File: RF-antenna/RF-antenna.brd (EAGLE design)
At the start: 108.2 x 108.2 mm, 7 parts, among them X1 SMA-V, X2 SMA-V, X3 SMA-V, X4 SMA-V, X5 SMA-V, X6 SMA-V

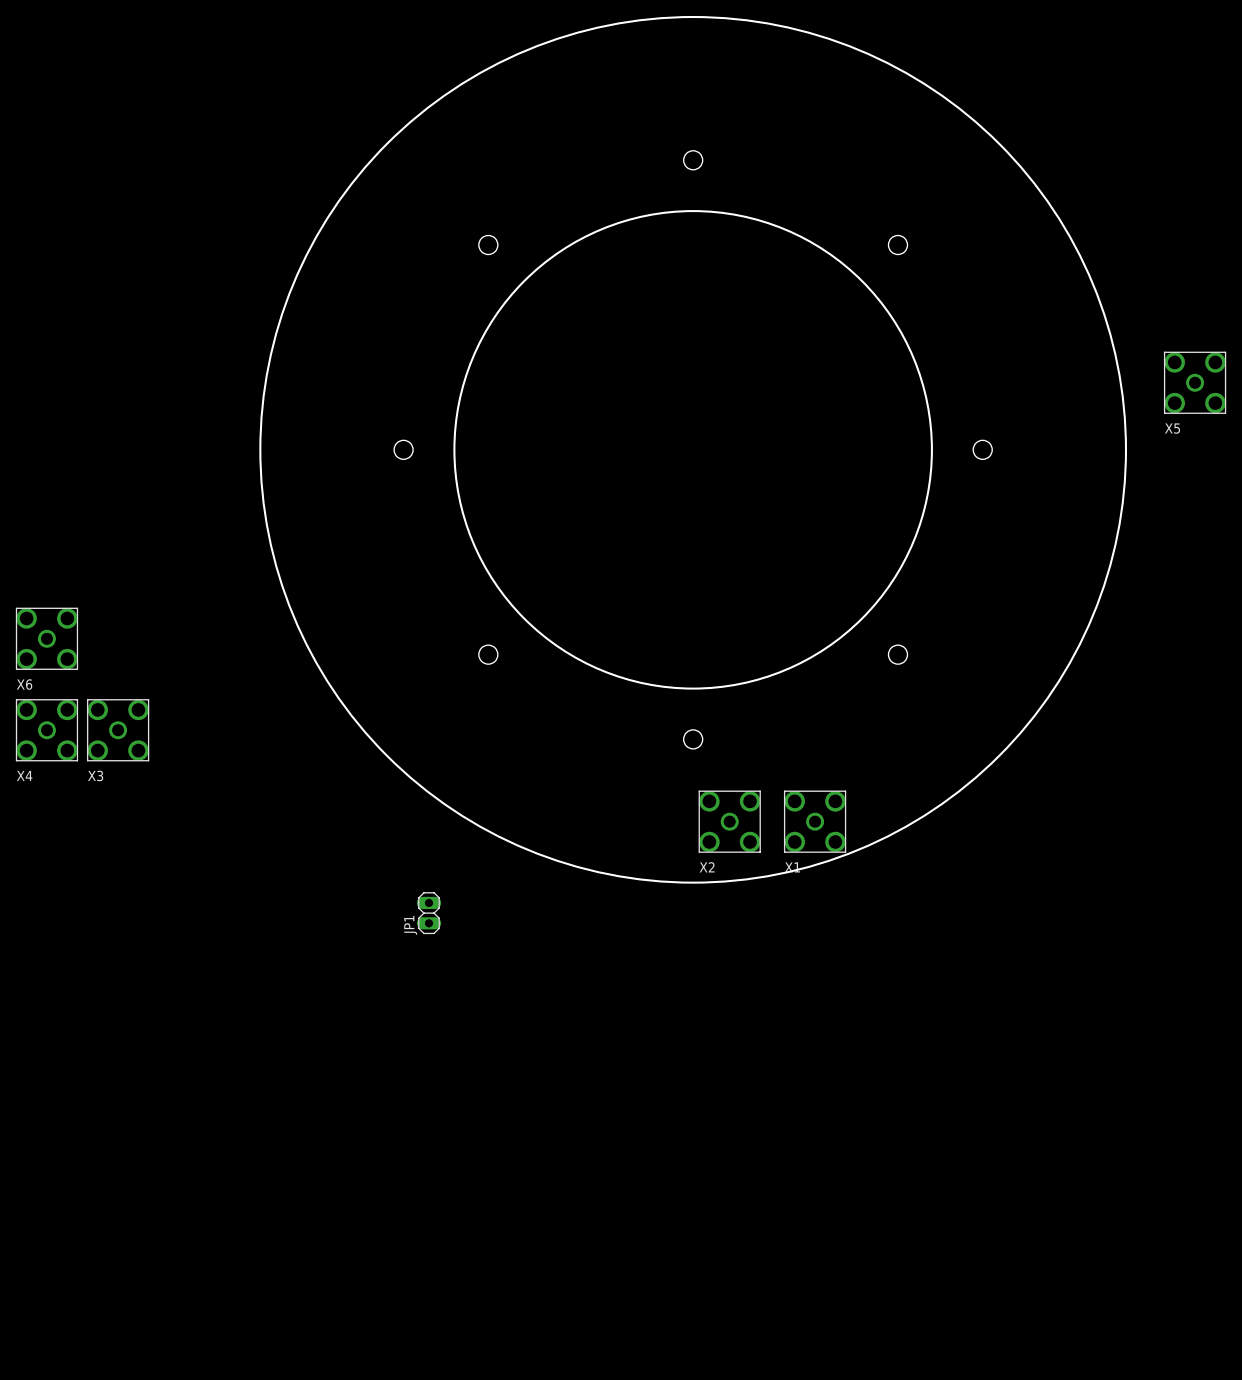
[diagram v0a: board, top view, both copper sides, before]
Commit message: Adding parts for footprinting
Added a bunch of test components to get an idea of how tight the design
will be. Also corrected the keepout areas.

DSB
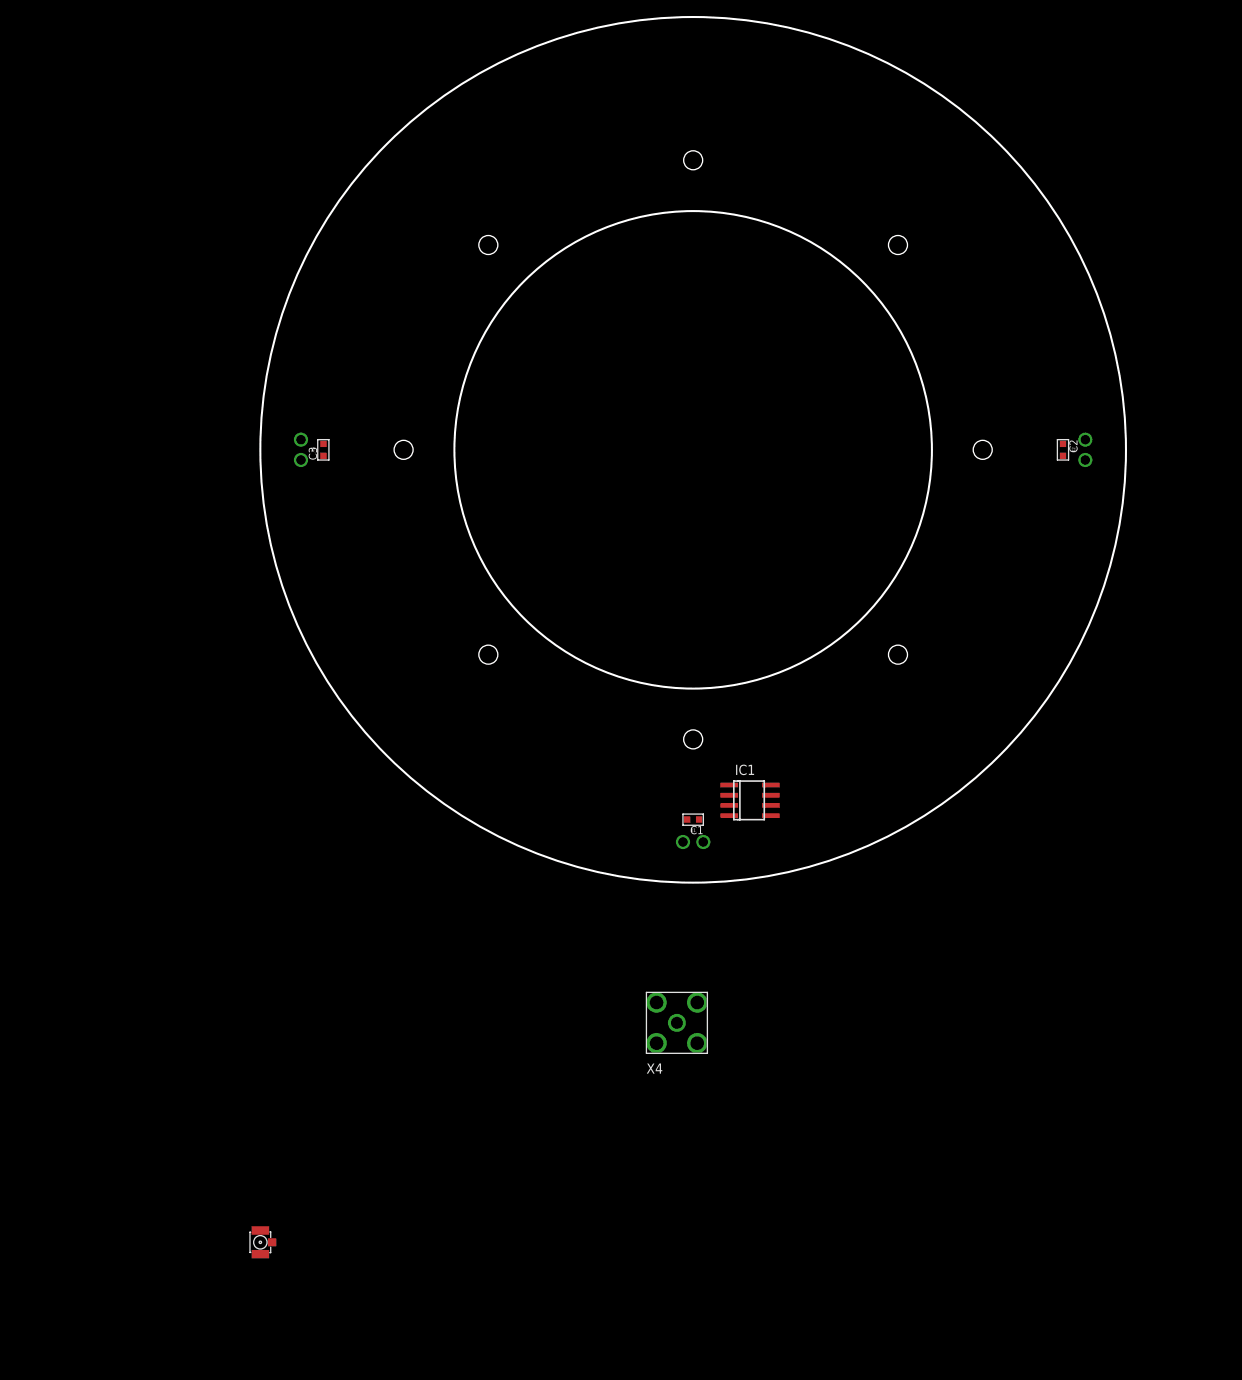
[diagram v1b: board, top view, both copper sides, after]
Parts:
- removed JP1: (no value), pinhead:1X02
- removed X5, X6: SMA-V, connector-jqi:SMA-V
- added C1, C2, C3: 5 pF, jqi_passives:C_MLCC_0603
- added CON1: UMC_CONNECTORREGULAR, qkdlab_alessandro:UMC_CONNECTOR
- added IC1: (no value), opamp-jqi:SO08
- X1, X2, X3: value SMA-V -> LG_HEADER; device connector-jqi:SMA-V -> connector-jqi:LG_HEADER
- moved X4 86.8 mm to (52.1, -17.5)
- moved X2 64.3 mm to (103.1, 54.1), turned to 90 degrees
- moved X3 41.8 mm to (5.08, 54.1), turned to 270 degrees
- moved X1 15.5 mm to (54.1, 5.08)
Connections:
- removed net GND: X1.GND1, X1.GND2, X1.GND3, X1.GND4, X2.GND1, X2.GND2, X2.GND3, X2.GND4
- new net N$2: C2.P$1, C2.P$2, X2.I, X2.R
- new net N$3: C3.P$1, C3.P$2, X3.I, X3.R
- new net V+: IC1.7
- new net V-: IC1.4
- net N$1: now also C1.P$1, C1.P$2, X1.I, X1.R; no longer X1.RF, X2.RF
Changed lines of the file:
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@@
 <?xml version="1.0" encoding="utf-8"?>
 <!DOCTYPE eagle SYSTEM "eagle.dtd">
-<eagle version="7.7.0">
+<eagle version="8.5.0">
 <drawing>
 <settings>
 <setting alwaysvectorfont="no"/>
+<setting keepoldvectorfont="yes"/>
 <setting verticaltext="up"/>
 </settings>
-<grid distance="0.01" unitdist="inch" unit="inch" style="lines" multiple="1" display="yes" altdistance="0.001" altunitdist="inch" altunit="inch"/>
+<grid distance="0.01" unitdist="inch" unit="inch" style="dots" multiple="1" display="yes" altdistance="0.001" altunitdist="inch" altunit="inch"/>
 <layers>
 <layer number="1" name="Top" color="4" fill="1" visible="yes" active="yes"/>
@@
 <circle x="54.102" y="54.102" radius="29.845" width="0.254" layer="20"/>
 <circle x="54.102" y="54.102" radius="54.102" width="0.254" layer="20"/>
-<wire x1="92.964" y1="54.102" x2="108.204" y2="61.722" width="0.254" layer="40"/>
-<wire x1="108.204" y1="61.722" x2="108.204" y2="46.482" width="0.254" layer="40"/>
-<wire x1="108.204" y1="46.482" x2="92.964" y2="54.102" width="0.254" layer="40"/>
-<wire x1="54.102" y1="92.964" x2="61.722" y2="108.204" width="0.254" layer="40"/>
-<wire x1="61.722" y1="108.204" x2="46.482" y2="108.204" width="0.254" layer="40"/>
-<wire x1="46.482" y1="108.204" x2="54.102" y2="92.964" width="0.254" layer="40"/>
-<wire x1="15.494" y1="54.102" x2="0" y2="46.482" width="0.254" layer="40"/>
-<wire x1="0" y1="46.482" x2="0" y2="61.722" width="0.254" layer="40"/>
-<wire x1="0" y1="61.722" x2="15.494" y2="54.102" width="0.254" layer="40"/>
-<wire x1="54.102" y1="15.494" x2="61.722" y2="0" width="0.254" layer="40"/>
-<wire x1="61.722" y1="0" x2="46.482" y2="0" width="0.254" layer="40"/>
-<wire x1="46.482" y1="0" x2="54.102" y2="15.494" width="0.254" layer="40"/>
 <hole x="90.297" y="54.102" drill="2.3749"/>
 <hole x="54.102" y="90.297" drill="2.3749"/>
@@
 <wire x1="70.104" y1="0" x2="70.104" y2="108.204" width="0.254" layer="39"/>
 <wire x1="70.104" y1="108.204" x2="38.1" y2="108.204" width="0.254" layer="39"/>
+<polygon width="0.254" layer="40" pour="hatch">
+<vertex x="96.774" y="60.96"/>
+<vertex x="106.934" y="66.04"/>
+<vertex x="107.188" y="65.024"/>
+<vertex x="107.442" y="63.754"/>
+<vertex x="107.696" y="62.23"/>
+<vertex x="107.95" y="60.706"/>
+<vertex x="108.204" y="57.912"/>
+<vertex x="108.204" y="54.102"/>
+<vertex x="108.204" y="50.292"/>
+<vertex x="107.95" y="47.752"/>
+<vertex x="107.696" y="45.974"/>
+<vertex x="107.442" y="44.45"/>
+<vertex x="107.188" y="43.18"/>
+<vertex x="106.934" y="42.164"/>
+<vertex x="96.774" y="47.244"/>
+<vertex x="97.028" y="49.276"/>
+<vertex x="97.282" y="52.832"/>
+<vertex x="97.282" y="54.102"/>
+<vertex x="97.282" y="55.372"/>
+<vertex x="97.028" y="58.928"/>
+</polygon>
+<polygon width="0.254" layer="40" pour="hatch">
+<vertex x="47.244" y="96.774"/>
+<vertex x="42.164" y="106.934"/>
+<vertex x="43.18" y="107.188"/>
+<vertex x="44.45" y="107.442"/>
+<vertex x="45.974" y="107.696"/>
+<vertex x="47.498" y="107.95"/>
+<vertex x="50.292" y="108.204"/>
+<vertex x="54.102" y="108.204"/>
+<vertex x="57.912" y="108.204"/>
+<vertex x="60.452" y="107.95"/>
+<vertex x="62.23" y="107.696"/>
+<vertex x="63.754" y="107.442"/>
+<vertex x="65.024" y="107.188"/>
+<vertex x="66.04" y="106.934"/>
+<vertex x="60.96" y="96.774"/>
+<vertex x="58.928" y="97.028"/>
+<vertex x="55.372" y="97.282"/>
+<vertex x="54.102" y="97.282"/>
+<vertex x="52.832" y="97.282"/>
+<vertex x="49.276" y="97.028"/>
+</polygon>
+<polygon width="0.254" layer="40" pour="hatch">
+<vertex x="11.43" y="47.244"/>
+<vertex x="1.27" y="42.164"/>
+<vertex x="1.016" y="43.18"/>
+<vertex x="0.762" y="44.45"/>
+<vertex x="0.508" y="45.974"/>
+<vertex x="0.254" y="47.498"/>
+<vertex x="0" y="50.292"/>
+<vertex x="0" y="54.102"/>
+<vertex x="0" y="57.912"/>
+<vertex x="0.254" y="60.452"/>
+<vertex x="0.508" y="62.23"/>
+<vertex x="0.762" y="63.754"/>
+<vertex x="1.016" y="65.024"/>
+<vertex x="1.27" y="66.04"/>
+<vertex x="11.43" y="60.96"/>
+<vertex x="11.176" y="58.928"/>
+<vertex x="10.922" y="55.372"/>
+<vertex x="10.922" y="54.102"/>
+<vertex x="10.922" y="52.832"/>
+<vertex x="11.176" y="49.276"/>
+</polygon>
+<polygon width="0.254" layer="40" pour="hatch">
+<vertex x="60.96" y="11.43"/>
+<vertex x="66.04" y="1.27"/>
+<vertex x="65.024" y="1.016"/>
+<vertex x="63.754" y="0.762"/>
+<vertex x="62.23" y="0.508"/>
+<vertex x="60.706" y="0.254"/>
+<vertex x="57.912" y="0"/>
+<vertex x="54.102" y="0"/>
+<vertex x="50.292" y="0"/>
+<vertex x="47.752" y="0.254"/>
+<vertex x="45.974" y="0.508"/>
+<vertex x="44.45" y="0.762"/>
+<vertex x="43.18" y="1.016"/>
+<vertex x="42.164" y="1.27"/>
+<vertex x="47.244" y="11.43"/>
+<vertex x="49.276" y="11.176"/>
+<vertex x="52.832" y="10.922"/>
+<vertex x="54.102" y="10.922"/>
+<vertex x="55.372" y="10.922"/>
+<vertex x="58.928" y="11.176"/>
+</polygon>
 </plain>
 <attributes>
@@
 <param name="dpMaxLengthDifference" value="10mm"/>
 <param name="dpGapFactor" value="2.5"/>
-<param name="checkGrid" value="0"/>
 <param name="checkAngle" value="0"/>
 <param name="checkFont" value="1"/>
 <param name="checkRestrict" value="1"/>
+<param name="checkStop" value="0"/>
+<param name="checkValues" value="0"/>
 <param name="useDiameter" value="13"/>
 <param name="maxErrors" value="50"/>
@@
 </autorouter>
 <elements>
-<element name="X1" library="connector-jqi" package="SMA-V" value="SMA-V" x="69.342" y="7.62"/>
-<element name="X2" library="connector-jqi" package="SMA-V" value="SMA-V" x="58.674" y="7.62"/>
-<element name="X3" library="connector-jqi" package="SMA-V" value="SMA-V" x="-17.78" y="19.05"/>
-<element name="X4" library="connector-jqi" package="SMA-V" value="SMA-V" x="-26.67" y="19.05"/>
-<element name="X5" library="connector-jqi" package="SMA-V" value="SMA-V" x="116.84" y="62.484"/>
-<element name="X6" library="connector-jqi" package="SMA-V" value="SMA-V" x="-26.67" y="30.48"/>
-<element name="JP1" library="pinhead" package="1X02" value="" x="21.082" y="-3.81" rot="R90"/>
+<element name="X1" library="connector-jqi" package="LG_HEADER" value="LG_HEADER" x="54.102" y="5.08"/>
+<element name="X2" library="connector-jqi" package="LG_HEADER" value="LG_HEADER" x="103.124" y="54.102" rot="R90"/>
+<element name="X3" library="connector-jqi" package="LG_HEADER" value="LG_HEADER" x="5.08" y="54.102" rot="R270"/>
+<element name="C1" library="jqi_passives" package="C_MLCC_0603" value="5 pF" x="54.102" y="7.874" rot="R180"/>
+<element name="C2" library="jqi_passives" package="C_MLCC_0603" value="5 pF" x="100.33" y="54.102" rot="R270"/>
+<element name="C3" library="jqi_passives" package="C_MLCC_0603" value="5 pF" x="7.874" y="54.102" rot="R90"/>
+<element name="X4" library="connector-jqi" package="SMA-V" value="SMA-V" x="52.07" y="-17.526"/>
+<element name="IC1" library="opamp-jqi" package="SO08" value="" x="61.214" y="10.922"/>
+<element name="CON1" library="qkdlab_alessandro" package="UMC_CONNECTOR" value="UMC_CONNECTORREGULAR" x="0" y="-44.958"/>
 </elements>
 <signals>
 <signal name="N$1">
-<contactref element="X1" pad="RF"/>
-<contactref element="X2" pad="RF"/>
-<wire x1="69.342" y1="7.62" x2="58.674" y2="7.62" width="0" layer="19" extent="1-1"/>
+<contactref element="X1" pad="I"/>
+<contactref element="X1" pad="R"/>
+<contactref element="C1" pad="P$2"/>
+<contactref element="C1" pad="P$1"/>
+<wire x1="52.832" y1="5.08" x2="55.372" y2="5.08" width="0" layer="19" extent="1-1"/>
+<wire x1="53.352" y1="7.874" x2="52.832" y2="5.08" width="0" layer="19" extent="1-1"/>
+<wire x1="54.852" y1="7.874" x2="53.352" y2="7.874" width="0" layer="19" extent="1-1"/>
 </signal>
-<signal name="GND">
-<contactref element="X1" pad="GND1"/>
-<contactref element="X1" pad="GND2"/>
-<contactref element="X1" pad="GND3"/>
-<contactref element="X1" pad="GND4"/>
-<contactref element="X2" pad="GND1"/>
-<contactref element="X2" pad="GND2"/>
-<contactref element="X2" pad="GND3"/>
-<contactref element="X2" pad="GND4"/>
-<wire x1="56.134" y1="10.16" x2="56.134" y2="5.08" width="0" layer="19" extent="1-1"/>
-<wire x1="61.214" y1="5.08" x2="56.134" y2="5.08" width="0" layer="19" extent="1-1"/>
-<wire x1="66.802" y1="5.08" x2="61.214" y2="5.08" width="0" layer="19" extent="1-1"/>
-<wire x1="61.214" y1="10.16" x2="56.134" y2="10.16" width="0" layer="19" extent="1-1"/>
-<wire x1="66.802" y1="10.16" x2="61.214" y2="10.16" width="0" layer="19" extent="1-1"/>
-<wire x1="71.882" y1="5.08" x2="66.802" y2="5.08" width="0" layer="19" extent="1-1"/>
-<wire x1="71.882" y1="10.16" x2="66.802" y2="10.16" width="0" layer="19" extent="1-1"/>
+<signal name="N$2">
+<contactref element="X2" pad="I"/>
+<contactref element="X2" pad="R"/>
+<contactref element="C2" pad="P$2"/>
+<contactref element="C2" pad="P$1"/>
+<wire x1="103.124" y1="52.832" x2="103.124" y2="55.372" width="0" layer="19" extent="1-1"/>
+<wire x1="100.33" y1="53.352" x2="103.124" y2="52.832" width="0" layer="19" extent="1-1"/>
+<wire x1="100.33" y1="54.852" x2="100.33" y2="53.352" width="0" layer="19" extent="1-1"/>
+</signal>
+<signal name="N$3">
+<contactref element="X3" pad="I"/>
+<contactref element="X3" pad="R"/>
+<contactref element="C3" pad="P$2"/>
+<contactref element="C3" pad="P$1"/>
+<wire x1="5.08" y1="52.832" x2="5.08" y2="55.372" width="0" layer="19" extent="1-1"/>
+<wire x1="7.874" y1="54.852" x2="5.08" y2="52.832" width="0" layer="19" extent="1-1"/>
+<wire x1="7.874" y1="53.352" x2="7.874" y2="54.852" width="0" layer="19" extent="1-1"/>
+</signal>
+<signal name="V+">
+<contactref element="IC1" pad="7"/>
+</signal>
+<signal name="V-">
+<contactref element="IC1" pad="4"/>
 </signal>
 </signals>
